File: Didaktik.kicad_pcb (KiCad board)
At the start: 2 copper layers, 102 parts, among them J1 USB_C_Receptacle_USB2.0, SW1 SW_Push, SW10 SW_Push_45deg, SW11 SW_Push_45deg, SW12 SW_Push_45deg, SW13 SW_Push_45deg, SW14 SW_Push_45deg, SW15 SW_Push_45deg, SW16 SW_Push_45deg, SW17 SW_Push_45deg, SW18 SW_Push_45deg, SW19 SW_Push_45deg, SW2 SW_Push_45deg, SW20 SW_Push_45deg, SW21 SW_Push_45deg, SW22 SW_Push_45deg, SW23 SW_Push_45deg, SW24 SW_Push_45deg, SW25 SW_Push_45deg, SW26 SW_Push_45deg, SW27 SW_Push_45deg, SW28 SW_Push_45deg, SW29 SW_Push_45deg, SW3 SW_Push_45deg, SW30 SW_Push_45deg, SW31 SW_Push_45deg, SW32 SW_Push_45deg, SW33 SW_Push_45deg, SW34 SW_Push_45deg, SW35 SW_Push_45deg, SW36 SW_Push_45deg, SW37 SW_Push_45deg, SW38 SW_Push_45deg, SW39 SW_Push_45deg, SW4 SW_Push_45deg, SW40 SW_Push_45deg, SW41 SW_Push_45deg, SW5 SW_Push_45deg, SW6 SW_Push_45deg, SW7 SW_Push_45deg, SW8 SW_Push_45deg, SW9 SW_Push_45deg, U1 ATmega32U4-M, Y1 Crystal_GND24_Small

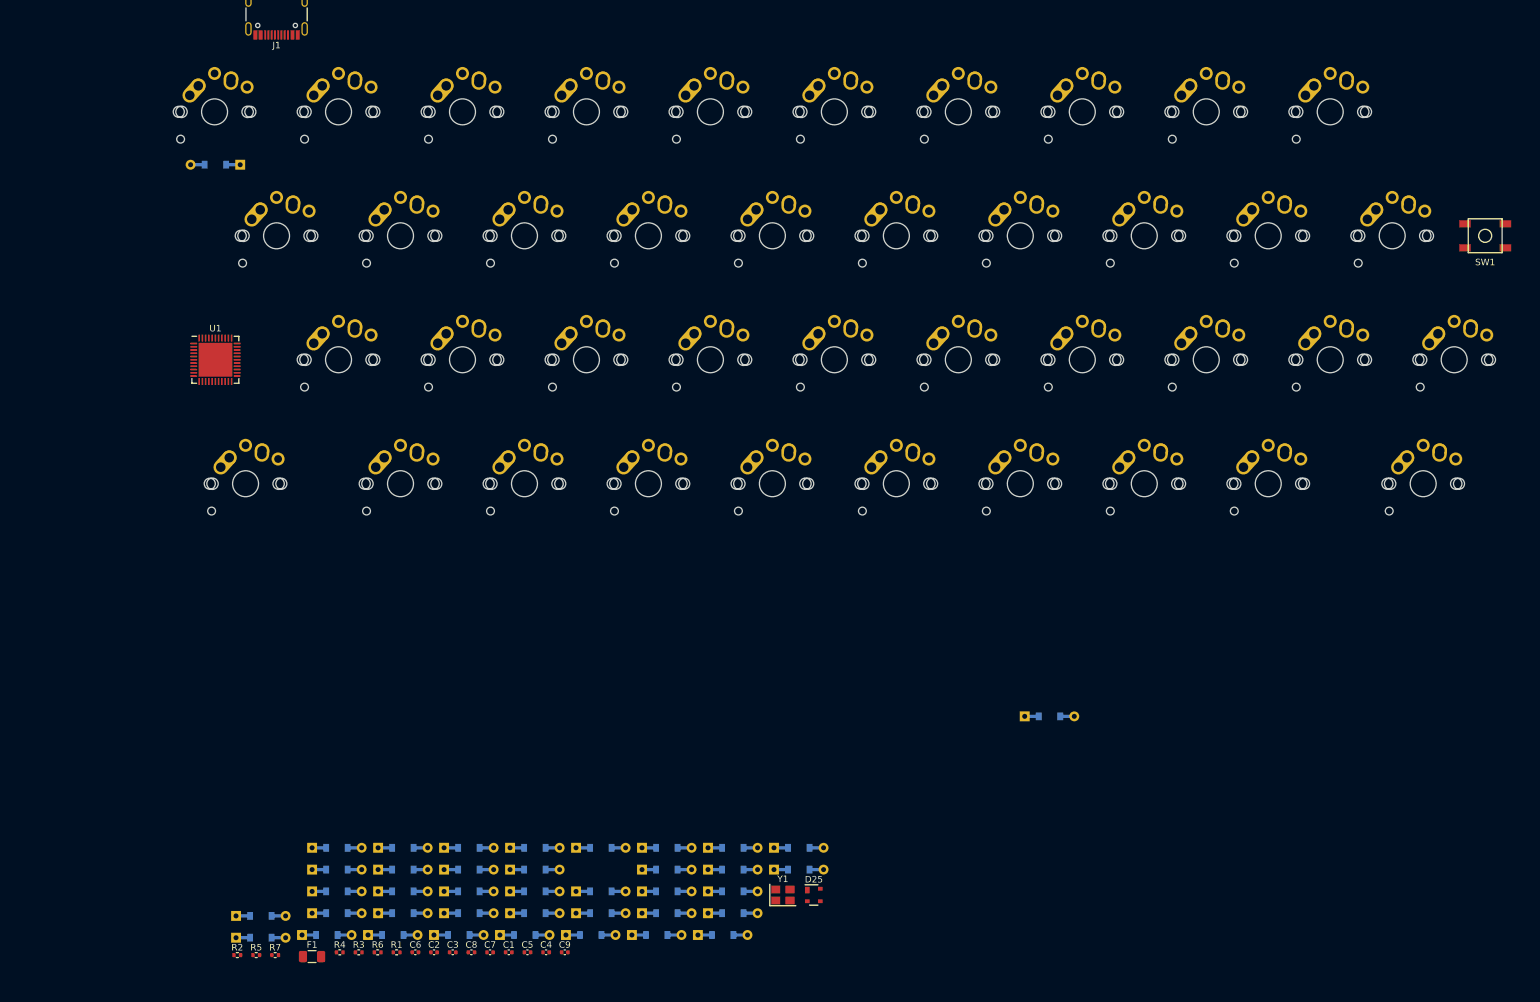
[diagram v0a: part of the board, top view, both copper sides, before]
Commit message: switch placement done, basic matrix routing done
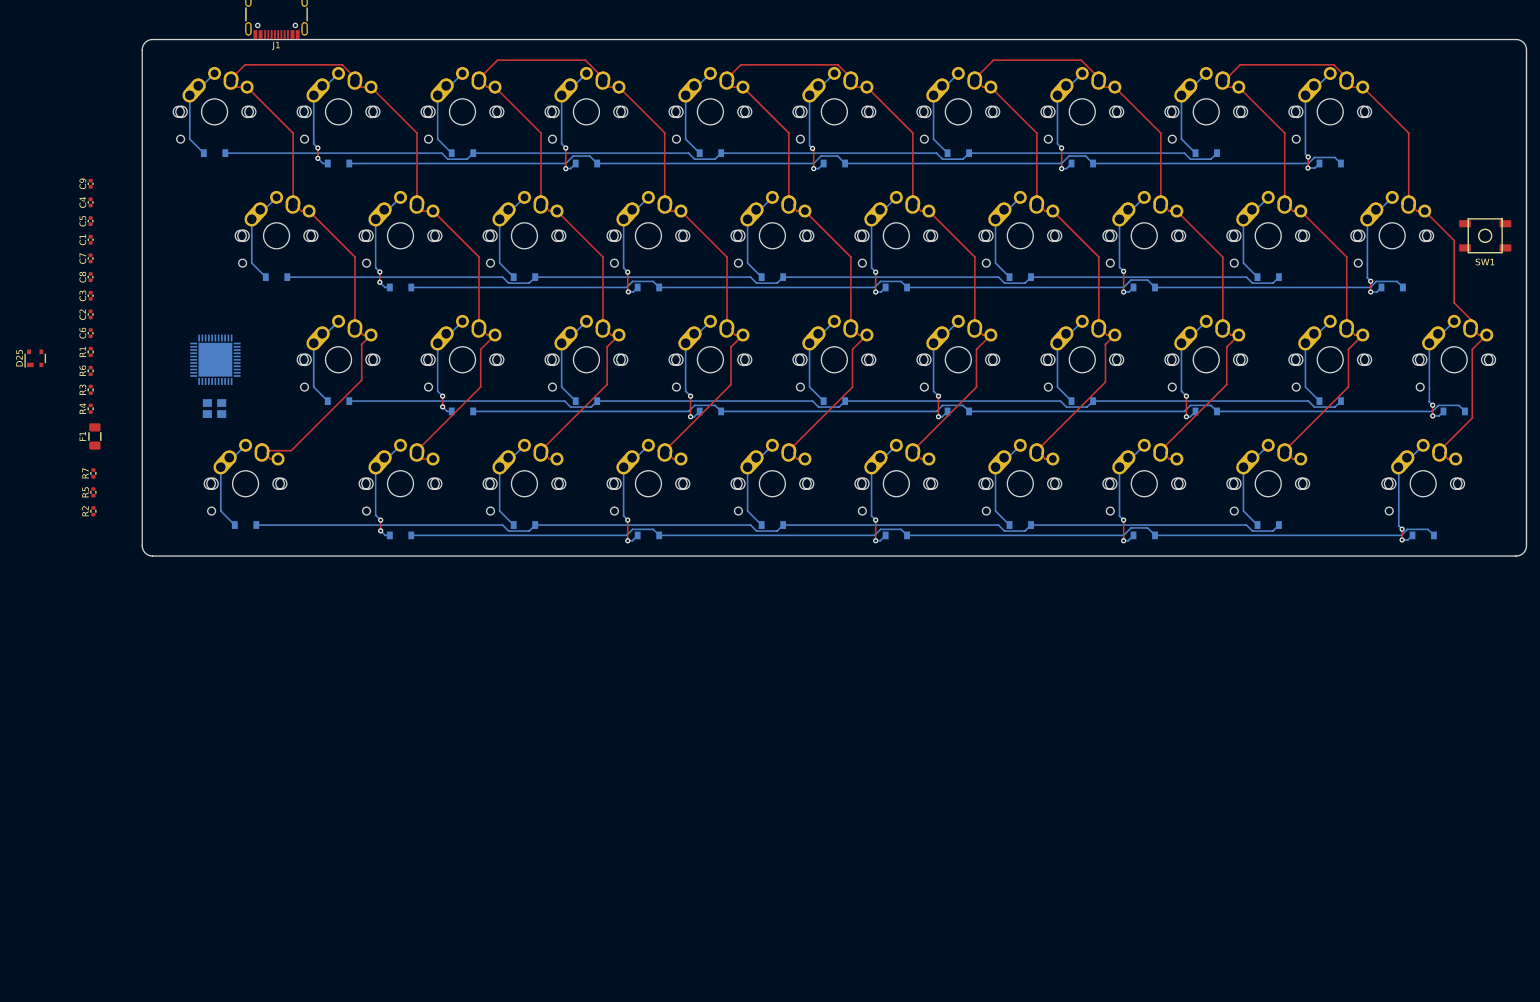
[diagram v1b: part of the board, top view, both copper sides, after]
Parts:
- D1, D10, D11, D12, D13, D14, D15, D16, D17, D18, D19, D2, D20, D21, D22, D23, D24, D26, D27, D28, D29, D3, D30, D31, D32, D33, D34, D35, D36, D37, D38, D39, D4, D40, D41, D5, D6, D7, D8, D9: footprint combodiode:ComboDiode -> Diode_SMD:D_SOD-123; moved to B.Cu
- U1, Y1: moved to B.Cu
- moved D40 181.9 mm to (231.8, 87.3), turned to 180 degrees
- moved D38 168.0 mm to (212.7, 49.2), turned to 180 degrees
- moved D36 158.2 mm to (212.7, 85.7), turned to 180 degrees
- moved D39 155.0 mm to (222.2, 68.3), turned to 180 degrees
- moved D25 145.3 mm to (13.7, 79.2), turned to 90 degrees
- moved D31 144.9 mm to (184.2, 68.3), turned to 180 degrees
- moved D26 139.3 mm to (155.6, 47.6), turned to 180 degrees
- moved C9 138.8 mm to (22.2, 52.3), turned to 90 degrees
- moved D34 137.6 mm to (193.7, 47.6), turned to 180 degrees
- moved C4 134.8 mm to (22.2, 55.2), turned to 90 degrees
- moved D30 134.1 mm to (174.6, 49.2), turned to 180 degrees
- moved C5 130.9 mm to (22.2, 58.1), turned to 90 degrees
- moved D28 128.8 mm to (174.6, 85.7), turned to 180 degrees
- moved C1 127.0 mm to (22.2, 60.9), turned to 90 degrees
- moved D22 126.5 mm to (146.1, 68.3), turned to 180 degrees
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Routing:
- net COL0: track 0.00 -> 177.5 mm
- net COL1: track 0.00 -> 174.4 mm
- net COL3: track 0.00 -> 174.0 mm
- net COL2: track 0.00 -> 173.3 mm
- net COL4: track 0.00 -> 171.6 mm
- net ROW7: track 0.00 -> 160.4 mm
- net ROW6: track 0.00 -> 160.2 mm
- net ROW1: track 0.00 -> 156.0 mm
- net ROW3: track 0.00 -> 155.6 mm
- net ROW4: track 0.00 -> 155.5 mm
- net ROW5: track 0.00 -> 155.5 mm
- net ROW0: track 0.00 -> 155.5 mm
- net ROW2: track 0.00 -> 155.5 mm
- net Net-(D21-Pad2): track 0.00 -> 18.7 mm, vias 0 -> 2
- net Net-(D13-Pad2): track 0.00 -> 18.7 mm, vias 0 -> 2
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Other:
- board outline added: 212.7 x 79.4 mm

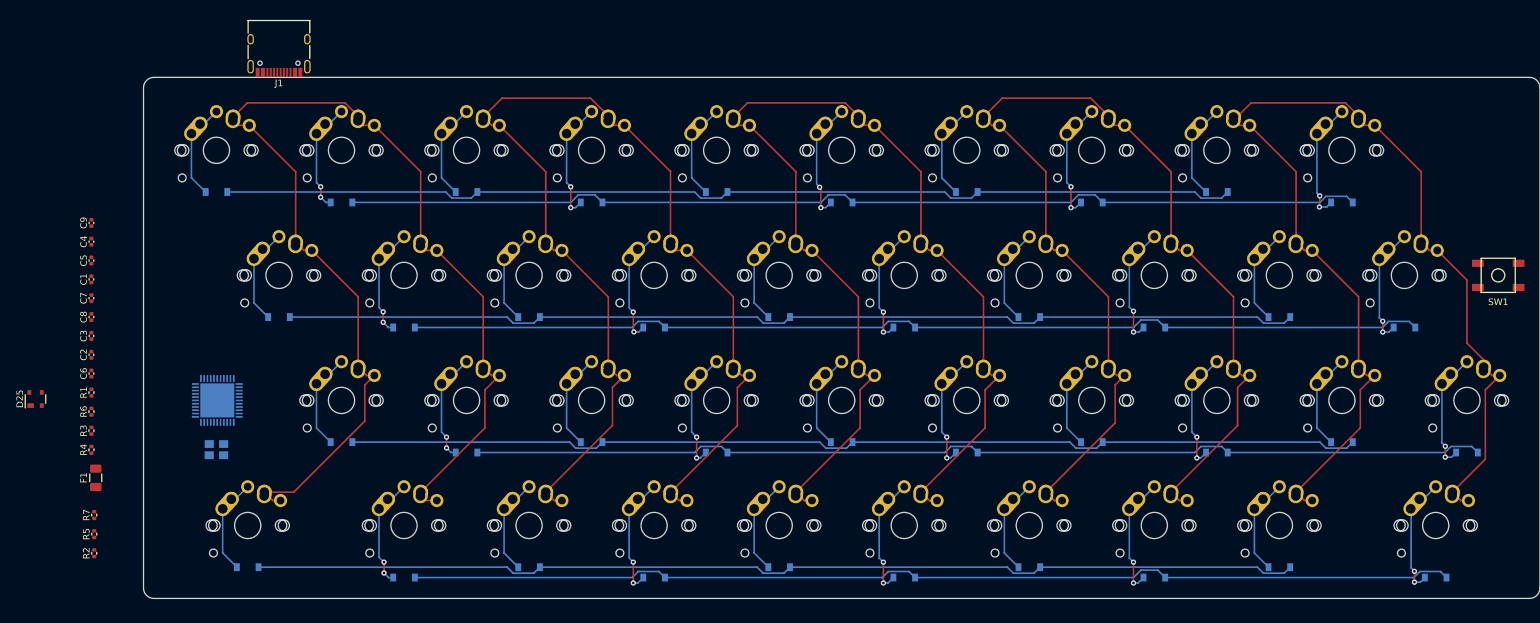
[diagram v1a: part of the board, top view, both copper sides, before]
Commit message: added jts, started to arrange MCU components
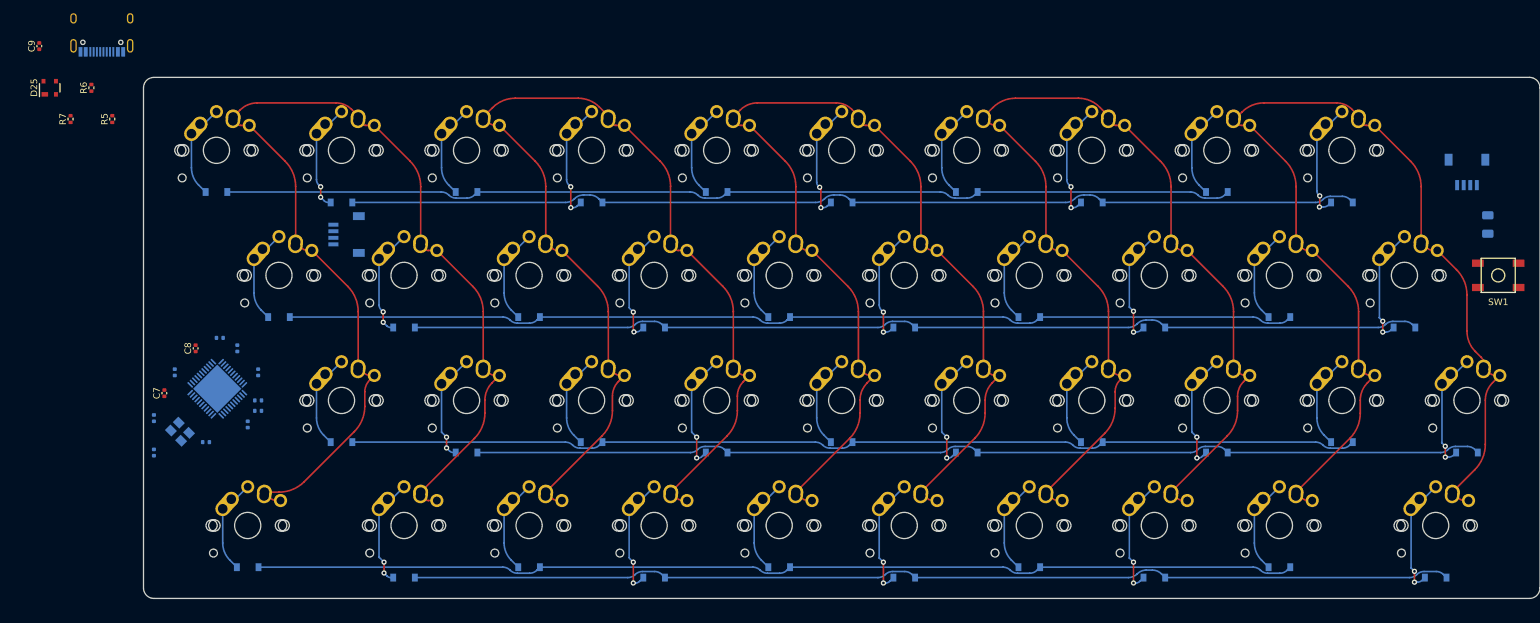
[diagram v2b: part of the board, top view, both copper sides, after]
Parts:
- added J2: Conn_01x04_MountingPin, random-keyboard-parts:JST-SR-4, B.Cu at (63.9, 54.1)
- added J2: Conn_01x04_MountingPin, random-keyboard-parts:JST-SR-4, B.Cu at (231.8, 41.8)
- C1, C2, C3, C4, C5, C6, F1, J1, R1, R2, R3, R4: moved to B.Cu
- moved F1 215.5 mm to (234.9, 52.6)
- moved R5 63.3 mm to (25.4, 36.5)
- moved R7 60.4 mm to (19.1, 36.5)
- moved R6 49.3 mm to (22.2, 31.8)
- moved D25 47.5 mm to (15.9, 31.8)
- moved C4 33.5 mm to (31.8, 87.3), turned to -90 degrees
- moved R2 33.1 mm to (47.6, 81.0), turned to 180 degrees
- moved C1 29.1 mm to (47.6, 75.1)
- moved C9 28.1 mm to (14.3, 25.4)
- moved J1 27.2 mm to (23.8, 22.2), turned to 0 degrees
- moved R4 25.9 mm to (41.8, 69.8), turned to 0 degrees
- moved C5 25.9 mm to (44.5, 71.4)
- moved R1 25.4 mm to (47.6, 79.4), turned to 180 degrees
- moved C6 25.0 mm to (46.0, 83.0)
- moved C7 18.2 mm to (33.3, 78.3)
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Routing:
- net COL4: track 171.6 -> 166.5 mm
- net COL1: track 174.4 -> 169.7 mm
- net COL2: track 173.3 -> 169.8 mm
- net COL3: track 174.0 -> 170.7 mm
- net COL0: track 177.5 -> 174.3 mm
- net ROW1: track 156.0 -> 154.9 mm
- net ROW7: track 160.4 -> 159.4 mm
- net ROW3: track 155.6 -> 154.7 mm
- net ROW6: track 160.2 -> 159.3 mm
- net ROW0: track 155.5 -> 154.6 mm
- net ROW4: track 155.5 -> 154.6 mm
- net ROW2: track 155.5 -> 154.6 mm
- net ROW5: track 155.5 -> 154.6 mm

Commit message: added leds
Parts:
- removed the J2 at (231.8, 41.8)
- added C10: C_Small, Capacitor_SMD:C_0402_1005Metric, F.Cu at (261.5, 46.0)
- added C11: C_Small, Capacitor_SMD:C_0402_1005Metric, F.Cu at (260.4, 42.3)
- added D42: LED, Keebio-Parts:LED_3mm, F.Cu at (236.5, 46.0)
- added D43: LED, Keebio-Parts:LED_3mm, F.Cu at (236.5, 39.0)
- added R8: R_Small, Resistor_SMD:R_0402_1005Metric, B.Cu at (239.7, 44.5)
- added R9: R_Small, Resistor_SMD:R_0402_1005Metric, B.Cu at (239.7, 39.2)
- C7, C8, D25: moved to B.Cu
- moved D25 213.6 mm to (228.6, 51.1), turned to 180 degrees
- moved J2 165.2 mm to (228.6, 41.7), turned to 0 degrees
- moved F1 13.1 mm to (222.2, 49.2), turned to -90 degrees
- moved SW1 4.76 mm to (236.5, 55.6)

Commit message: cleaned schematics, continued routing
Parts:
- removed C10, C11: C_Small, Capacitor_SMD:C_0402_1005Metric
- removed C9: 4.7nF, Capacitor_SMD:C_0402_1005Metric
- removed J1: USB_C_Receptacle_USB2.0, Connector_USB:USB_C_Receptacle_HRO_TYPE-C-31-M-12
- removed R5: 1M, Resistor_SMD:R_0402_1005Metric
- removed R6, R7: 5.1k, Resistor_SMD:R_0402_1005Metric
- moved F1 9.53 mm to (231.8, 49.0)
- moved D25 5.29 mm to (227.5, 45.9), turned to 0 degrees
- moved J2 5.29 mm to (227.5, 36.5)
- moved C3 4.43 mm to (35.7, 84.2), turned to 45 degrees
- moved C4 4.04 mm to (35.6, 88.6), turned to -45 degrees
- moved R3 3.39 mm to (42.9, 84.7), turned to 45 degrees
- moved Y1 3.12 mm to (38.0, 86.2)
- moved R1 1.79 mm to (49.4, 79.2)
- moved R2 1.79 mm to (49.4, 80.8)
- moved R4 0.40 mm to (41.7, 70.2)
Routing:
- net ROW6: track 159.3 -> 374.8 mm, vias 0 -> 2
- net ROW4: track 154.6 -> 364.1 mm, vias 0 -> 2
- net ROW2: track 154.6 -> 355.4 mm, vias 0 -> 2
- net D+: track 0.00 -> 197.1 mm
- net ROW0: track 154.6 -> 351.4 mm, vias 0 -> 2
- net D-: track 0.00 -> 196.3 mm
- net ROW7: track 159.4 -> 347.8 mm
- net ROW5: track 154.6 -> 342.7 mm
- net ROW3: track 154.7 -> 333.3 mm
- net ROW1: track 154.9 -> 330.1 mm
- net GND: track 0.00 -> 26.2 mm
- net Net-(C4-Pad2): track 0.00 -> 15.1 mm
- net COL1: track 169.7 -> 180.1 mm
- net COL4: track 166.5 -> 176.9 mm
- net COL2: track 169.8 -> 180.3 mm
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
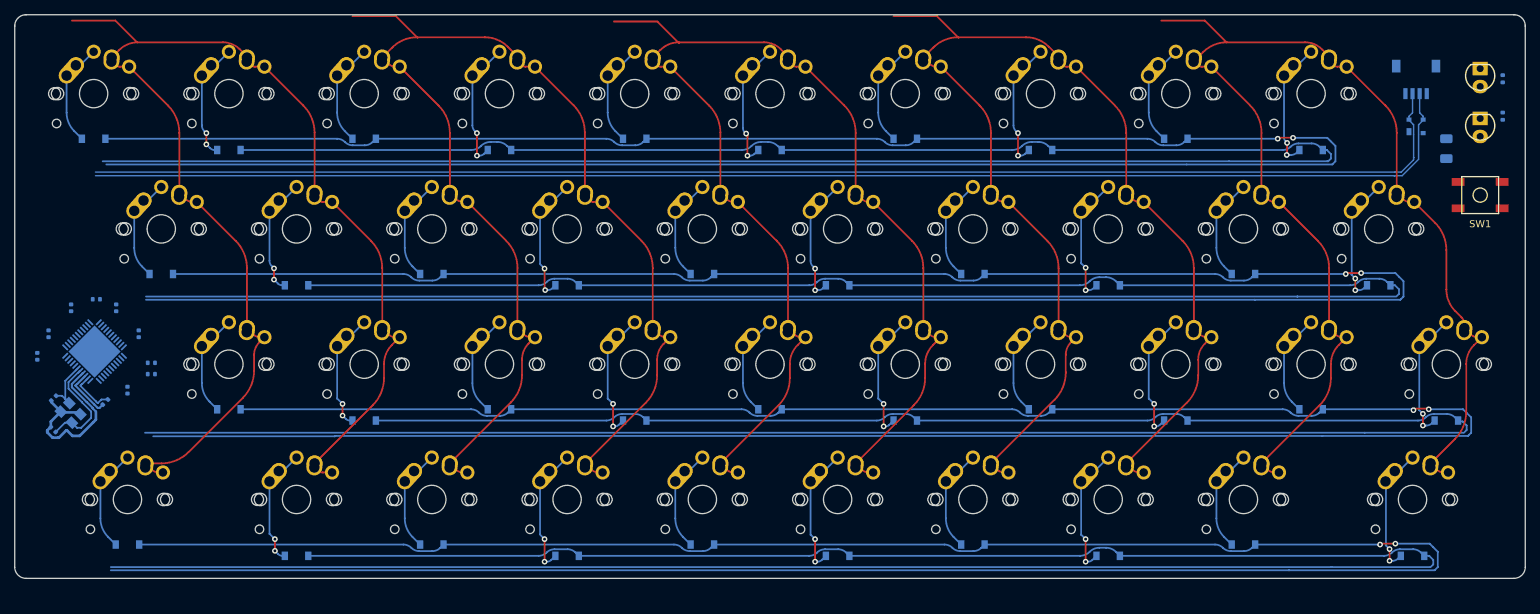
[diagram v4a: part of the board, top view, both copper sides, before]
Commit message: all traces routed, schematics cleaned up
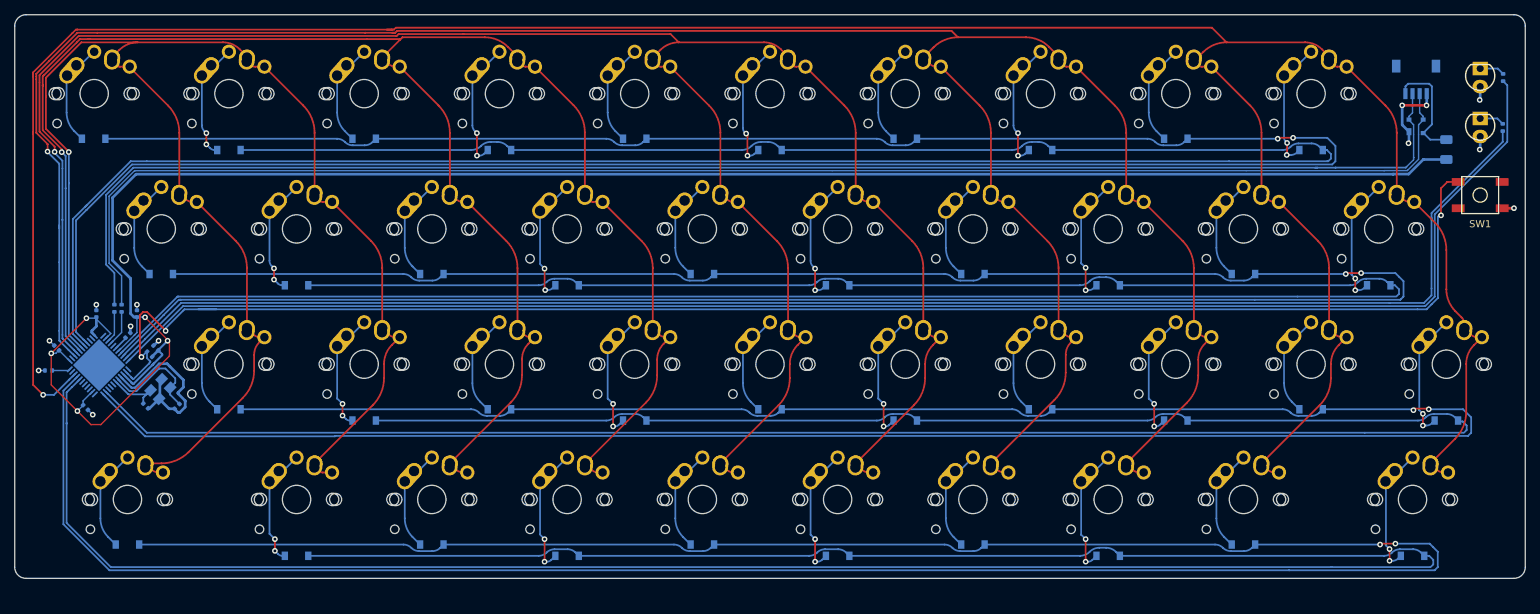
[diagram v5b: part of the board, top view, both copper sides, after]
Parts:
- moved C4 17.7 mm to (53.0, 85.3), turned to 45 degrees
- moved C7 16.7 mm to (50.0, 77.1), turned to 135 degrees
- moved Y1 13.1 mm to (50.7, 82.9), turned to 45 degrees
- moved C3 13.0 mm to (48.6, 85.3), turned to 135 degrees
- moved R4 12.1 mm to (34.9, 80.3), turned to 180 degrees
- moved C2 11.6 mm to (40.1, 85.5), turned to -45 degrees
- moved R2 10.2 mm to (45.2, 71.5), turned to -90 degrees
- moved C5 10.1 mm to (36.1, 77.1), turned to 135 degrees
- moved C8 9.31 mm to (47.4, 72.3)
- moved R1 9.28 mm to (44.2, 71.5), turned to -90 degrees
- moved R3 9.17 mm to (49.1, 78.0), turned to 135 degrees
- moved C6 7.72 mm to (46.1, 75.3), turned to 45 degrees
- moved C1 6.61 mm to (41.7, 72.3)
- moved U1 2.01 mm to (42.0, 79.5), turned to -135 degrees
- moved R8 1.59 mm to (239.7, 46.0)
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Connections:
- U1 pad 10: unconnected-(U1-Pad10) -> LED Power
- U1 pad 11: unconnected-(U1-Pad11) -> LED capslock
- U1 pad 21: unconnected-(U1-Pad21) -> ROW5
- U1 pad 22: unconnected-(U1-Pad22) -> ROW4
- U1 pad 29: unconnected-(U1-Pad29) -> ROW7
- U1 pad 30: unconnected-(U1-Pad30) -> ROW6
- U1 pad 31: unconnected-(U1-Pad31) -> COL4
- U1 pad 36: unconnected-(U1-Pad36) -> COL3
- U1 pad 37: unconnected-(U1-Pad37) -> COL2
- U1 pad 38: unconnected-(U1-Pad38) -> COL1
- U1 pad 39: unconnected-(U1-Pad39) -> COL0
- U1 pad 40: unconnected-(U1-Pad40) -> ROW1
- U1 pad 41: unconnected-(U1-Pad41) -> ROW0
- U1 pad 8: unconnected-(U1-Pad8) -> ROW3
- U1 pad 9: unconnected-(U1-Pad9) -> ROW2
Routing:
- net +5V: track 7.30 -> 284.8 mm, vias 0 -> 5
- net LED capslock: track 0.00 -> 222.5 mm
- net LED Power: track 0.00 -> 215.2 mm
- net Net-(R3-Pad2): track 6.55 -> 221.2 mm, vias 0 -> 3
- net COL4: track 176.9 -> 390.7 mm, vias 0 -> 1
- net COL3: track 181.2 -> 346.0 mm, vias 0 -> 1
- net COL2: track 180.3 -> 304.1 mm, vias 0 -> 1
- net COL1: track 180.1 -> 263.6 mm, vias 0 -> 1
- net COL0: track 184.8 -> 229.6 mm, vias 0 -> 1
- net ROW6: track 374.8 -> 405.7 mm
- net ROW7: track 347.8 -> 377.7 mm
- net ROW1: track 330.1 -> 356.6 mm
- net ROW0: track 351.4 -> 376.9 mm
- net GND: track 26.2 -> 48.8 mm, vias 0 -> 13
- net D-: track 196.3 -> 212.3 mm
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
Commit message: full routing, silkscreens, zones
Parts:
- added G***: LOGO, LOGO, F.Cu at (136.5, 66.7)
- added G***: LOGO, LOGO, F.Cu at (136.5, 87.3)
- renumbered J2 to J1
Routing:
- added copper zone on B.Cu, net (none)
- added copper zone on F.Cu, net (none)
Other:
- board text added: "Didaktik 40 v1.0 by Calvin#0563"

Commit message: created switchplate 40, cleaned 40s pcb. finished schematics for 45. created pcb project for 45
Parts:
- R8, R9: value R_Small -> 220 ohm
- moved D25 1.92 mm to (227.5, 47.8)
- moved J1 1.92 mm to (227.5, 38.4)
- moved G*** 1.59 mm to (136.5, 65.1)
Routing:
- net D-: track 212.3 -> 210.3 mm
- net D+: track 212.3 -> 210.4 mm
